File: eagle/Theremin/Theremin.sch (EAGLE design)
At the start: 15 parts, among them Q6 2N3904, Q7 2N3904, Q8 2N3904

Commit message: get everything committed to move to new machine
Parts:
- added C13: 22uF, SparkFun-Capacitors:CAP_POLPTH4
- added C14: 1800pF, SparkFun-Capacitors:CAPPTH3
- added C15: 6800pF, capacitor-wima:C5/3
- added D1, D3: 1N4004, diode:1N4004
- added L11: 47uH, marky-parts:SLOT-TEN-SIMPLE
- added L14: 22uH, marky-parts:DELEVAN-FIXED-INDUCTOR
- added U1: LM78L12, marky-parts:LM78L12
- added U2: LM79L12, marky-parts:LM79L12
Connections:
- new net N$10: C13.+, L11.IN$1, Q7.C
- new net N$11: L11.OUT$2, L14.P$1
- new net N$12: D3.A, U2.VIN
- new net N$13: D1.C, U1.VIN
- net GND: now also C13.-, C15.2, L11.P$1, L11.P$2, R17.1, U1.GND, U2.GND
- net N$4: now also C14.1, L14.P$2, Q6.C
- net N$8: now also R15.2
- net N$9: now also C14.2, C15.1
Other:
- moved on the sheet: C16, C17, C18, Q6, Q7, Q8, R15, R16, R17, R18, R19, R20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

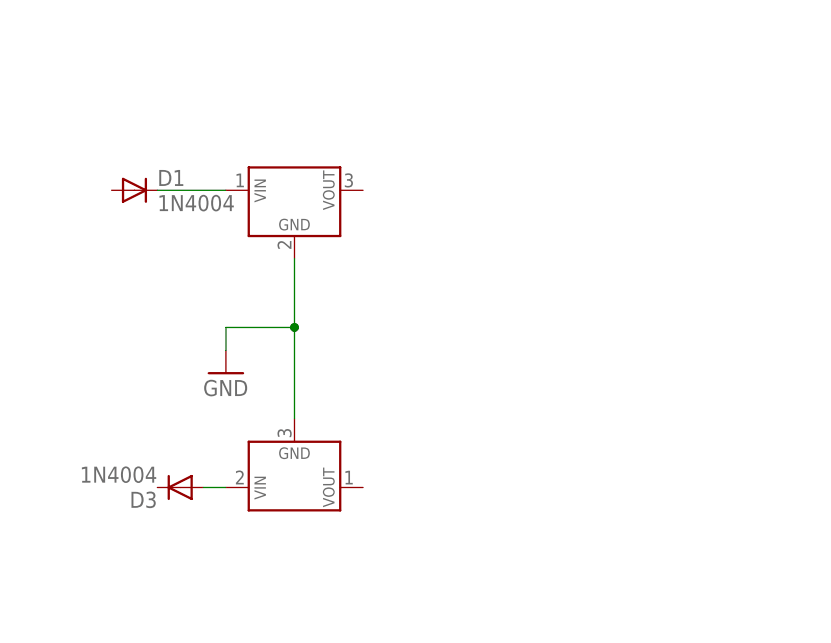
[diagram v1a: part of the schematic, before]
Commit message: Add big capacitors to theremin power supply
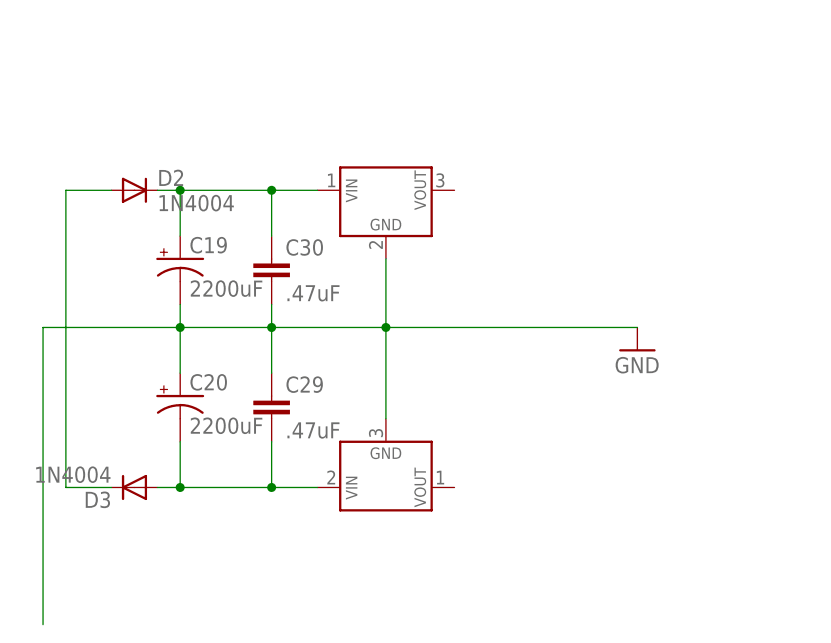
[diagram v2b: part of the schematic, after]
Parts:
- added C19, C20: 2200uF, marky-parts:1CM-RADIAL-CAP-POL
- added C29, C30: .47uF, SparkFun-Capacitors:CAP_
- renumbered D1 to D2
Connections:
- new net N$14: D2.A, D3.C
- net GND: now also C19.-, C20.+, C29.1, C30.2
- net N$12: now also C20.-, C29.2
- net N$13: now also C19.+, C30.1
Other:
- moved on the sheet: D3
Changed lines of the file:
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@@
 <setting verticaltext="up"/>
 </settings>
-<grid distance="0.1" unitdist="inch" unit="inch" style="lines" multiple="1" display="yes" altdistance="0.01" altunitdist="inch" altunit="inch"/>
+<grid distance="0.1" unitdist="inch" unit="inch" style="lines" multiple="1" display="no" altdistance="0.01" altunitdist="inch" altunit="inch"/>
 <layers>
 <layer number="1" name="Top" color="4" fill="1" visible="no" active="no"/>
@@
 <part name="U2" library="marky-parts" deviceset="LM79L12" device=""/>
 <part name="U1" library="marky-parts" deviceset="LM78L12" device=""/>
-<part name="D1" library="diode" deviceset="1N4004" device=""/>
+<part name="D2" library="diode" deviceset="1N4004" device=""/>
+<part name="C19" library="marky-parts" deviceset="1CM-RADIAL-CAP-POL" device="" value="2200uF"/>
+<part name="C20" library="marky-parts" deviceset="1CM-RADIAL-CAP-POL" device="" value="2200uF"/>
+<part name="C30" library="SparkFun-Capacitors" deviceset="CAP" device="_" value=".47uF"/>
+<part name="C29" library="SparkFun-Capacitors" deviceset="CAP" device="_" value=".47uF"/>
 </parts>
 <sheets>
@@
 <instance part="GND6" gate="1" x="157.48" y="120.65"/>
 <instance part="C14" gate="G$1" x="170.18" y="101.6"/>
-<instance part="D3" gate="1" x="17.78" y="43.18" rot="R180"/>
-<instance part="GND7" gate="1" x="22.86" y="55.88"/>
-<instance part="U2" gate="G$1" x="30.48" y="43.18"/>
-<instance part="U1" gate="G$1" x="30.48" y="76.2"/>
-<instance part="D1" gate="1" x="12.7" y="76.2"/>
+<instance part="D3" gate="1" x="12.7" y="43.18" rot="R180"/>
+<instance part="GND7" gate="1" x="68.58" y="58.42"/>
+<instance part="U2" gate="G$1" x="40.64" y="43.18"/>
+<instance part="U1" gate="G$1" x="40.64" y="76.2"/>
+<instance part="D2" gate="1" x="12.7" y="76.2"/>
+<instance part="C19" gate="G$1" x="17.78" y="68.58"/>
+<instance part="C20" gate="G$1" x="17.78" y="53.34"/>
+<instance part="C30" gate="G$1" x="27.94" y="66.04"/>
+<instance part="C29" gate="G$1" x="27.94" y="50.8"/>
 </instances>
 <busses>
@@
 <segment>
 <pinref part="U2" gate="G$1" pin="GND"/>
-<wire x1="30.48" y1="50.8" x2="30.48" y2="60.96" width="0.1524" layer="91"/>
-<wire x1="30.48" y1="60.96" x2="22.86" y2="60.96" width="0.1524" layer="91"/>
+<wire x1="40.64" y1="50.8" x2="40.64" y2="60.96" width="0.1524" layer="91"/>
 <pinref part="GND7" gate="1" pin="GND"/>
-<wire x1="22.86" y1="60.96" x2="22.86" y2="58.42" width="0.1524" layer="91"/>
+<wire x1="40.64" y1="60.96" x2="68.58" y2="60.96" width="0.1524" layer="91"/>
 <pinref part="U1" gate="G$1" pin="GND"/>
-<wire x1="30.48" y1="68.58" x2="30.48" y2="60.96" width="0.1524" layer="91"/>
-<junction x="30.48" y="60.96"/>
+<wire x1="40.64" y1="68.58" x2="40.64" y2="60.96" width="0.1524" layer="91"/>
+<junction x="40.64" y="60.96"/>
+<pinref part="C20" gate="G$1" pin="+"/>
+<pinref part="C19" gate="G$1" pin="-"/>
+<wire x1="17.78" y1="55.88" x2="17.78" y2="60.96" width="0.1524" layer="91"/>
+<wire x1="17.78" y1="60.96" x2="17.78" y2="63.5" width="0.1524" layer="91"/>
+<wire x1="40.64" y1="60.96" x2="27.94" y2="60.96" width="0.1524" layer="91"/>
+<wire x1="27.94" y1="60.96" x2="17.78" y2="60.96" width="0.1524" layer="91"/>
+<wire x1="17.78" y1="60.96" x2="2.54" y2="60.96" width="0.1524" layer="91"/>
+<wire x1="2.54" y1="60.96" x2="2.54" y2="27.94" width="0.1524" layer="91"/>
+<junction x="17.78" y="60.96"/>
+<pinref part="C29" gate="G$1" pin="1"/>
+<pinref part="C30" gate="G$1" pin="2"/>
+<wire x1="27.94" y1="55.88" x2="27.94" y2="60.96" width="0.1524" layer="91"/>
+<junction x="27.94" y="60.96"/>
+<wire x1="27.94" y1="60.96" x2="27.94" y2="63.5" width="0.1524" layer="91"/>
 </segment>
 </net>
@@
 <pinref part="U2" gate="G$1" pin="VIN"/>
 <pinref part="D3" gate="1" pin="A"/>
-<wire x1="22.86" y1="43.18" x2="20.32" y2="43.18" width="0.1524" layer="91"/>
+<wire x1="33.02" y1="43.18" x2="27.94" y2="43.18" width="0.1524" layer="91"/>
+<pinref part="C20" gate="G$1" pin="-"/>
+<wire x1="27.94" y1="43.18" x2="17.78" y2="43.18" width="0.1524" layer="91"/>
+<wire x1="17.78" y1="43.18" x2="15.24" y2="43.18" width="0.1524" layer="91"/>
+<wire x1="17.78" y1="48.26" x2="17.78" y2="43.18" width="0.1524" layer="91"/>
+<junction x="17.78" y="43.18"/>
+<pinref part="C29" gate="G$1" pin="2"/>
+<wire x1="27.94" y1="43.18" x2="27.94" y2="48.26" width="0.1524" layer="91"/>
+<junction x="27.94" y="43.18"/>
 </segment>
 </net>
 <net name="N$13" class="0">
 <segment>
-<pinref part="D1" gate="1" pin="C"/>
+<pinref part="D2" gate="1" pin="C"/>
 <pinref part="U1" gate="G$1" pin="VIN"/>
-<wire x1="15.24" y1="76.2" x2="22.86" y2="76.2" width="0.1524" layer="91"/>
-</segment>
-</net>
+<wire x1="15.24" y1="76.2" x2="17.78" y2="76.2" width="0.1524" layer="91"/>
+<pinref part="C19" gate="G$1" pin="+"/>
+<wire x1="17.78" y1="76.2" x2="27.94" y2="76.2" width="0.1524" layer="91"/>
+<wire x1="27.94" y1="76.2" x2="33.02" y2="76.2" width="0.1524" layer="91"/>
+<wire x1="17.78" y1="71.12" x2="17.78" y2="76.2" width="0.1524" layer="91"/>
+<junction x="17.78" y="76.2"/>
+<pinref part="C30" gate="G$1" pin="1"/>
+<wire x1="27.94" y1="71.12" x2="27.94" y2="76.2" width="0.1524" layer="91"/>
+<junction x="27.94" y="76.2"/>
+</segment>
+</net>
+<net name="N$14" class="0">
+<segment>
+<pinref part="D3" gate="1" pin="C"/>
+<wire x1="10.16" y1="43.18" x2="5.08" y2="43.18" width="0.1524" layer="91"/>
+<wire x1="5.08" y1="43.18" x2="5.08" y2="76.2" width="0.1524" layer="91"/>
+<pinref part="D2" gate="1" pin="A"/>
+<wire x1="5.08" y1="76.2" x2="10.16" y2="76.2" width="0.1524" layer="91"/>
+</segment>
+</net>

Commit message: Added Variable Pitch Oscillator cleaned up layout of schematic
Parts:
- added C1: 3300pF, marky-parts:CAP-9M-RADIAL
- added C2: 15pF, SparkFun-Capacitors:CAPPTH
- added C3: 0.01uF, marky-parts:CAP-5M-RADIAL
- added C4: 1uF, SparkFun-Passives:CAP_POLPTH2
- added L12: 47uH, marky-parts:DELEVAN-FIXED-INDUCTOR
- added L5: 47uH, marky-parts:SLOT-TEN-SIMPLE
- added Q1, Q2: 2N3904, transistor:2N3904
- added R1, R4: 1K, SparkFun-Resistors:RESISTORPTH-1/4W
- added R2: 2.2K, SparkFun-Resistors:RESISTORPTH-1/4W
- added R3: 47K, SparkFun-Resistors:RESISTORPTH-1/4W
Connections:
- new net 5V: C1.1, C13.+, C3.2, C4.+, L11.IN$1, L5.IN$1, Q2.C, Q7.C, R3.2
- new net N$16: Q1.B, R1.2
- new net N$17: C1.2, C2.1, C3.1, L12.P$2, Q1.C
- new net N$18: Q1.E, Q2.E, R2.2
- new net N$19: Q2.B, R3.1, R4.1
- new net N$20: C2.2
- net -12V: now also R2.1
- net GND: now also C4.-, L5.P$1, L5.P$2, R1.1, R4.2
- net N$10: now also L12.P$1, L5.OUT$2; no longer C13.+, L11.IN$1, Q7.C
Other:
- note added: "Power Supply"
- note added: "VARIABLE PITCH OSCILLATOR"
- note added: "Volume Antenna Circuit"
- note added: "to Pitch Antenna"

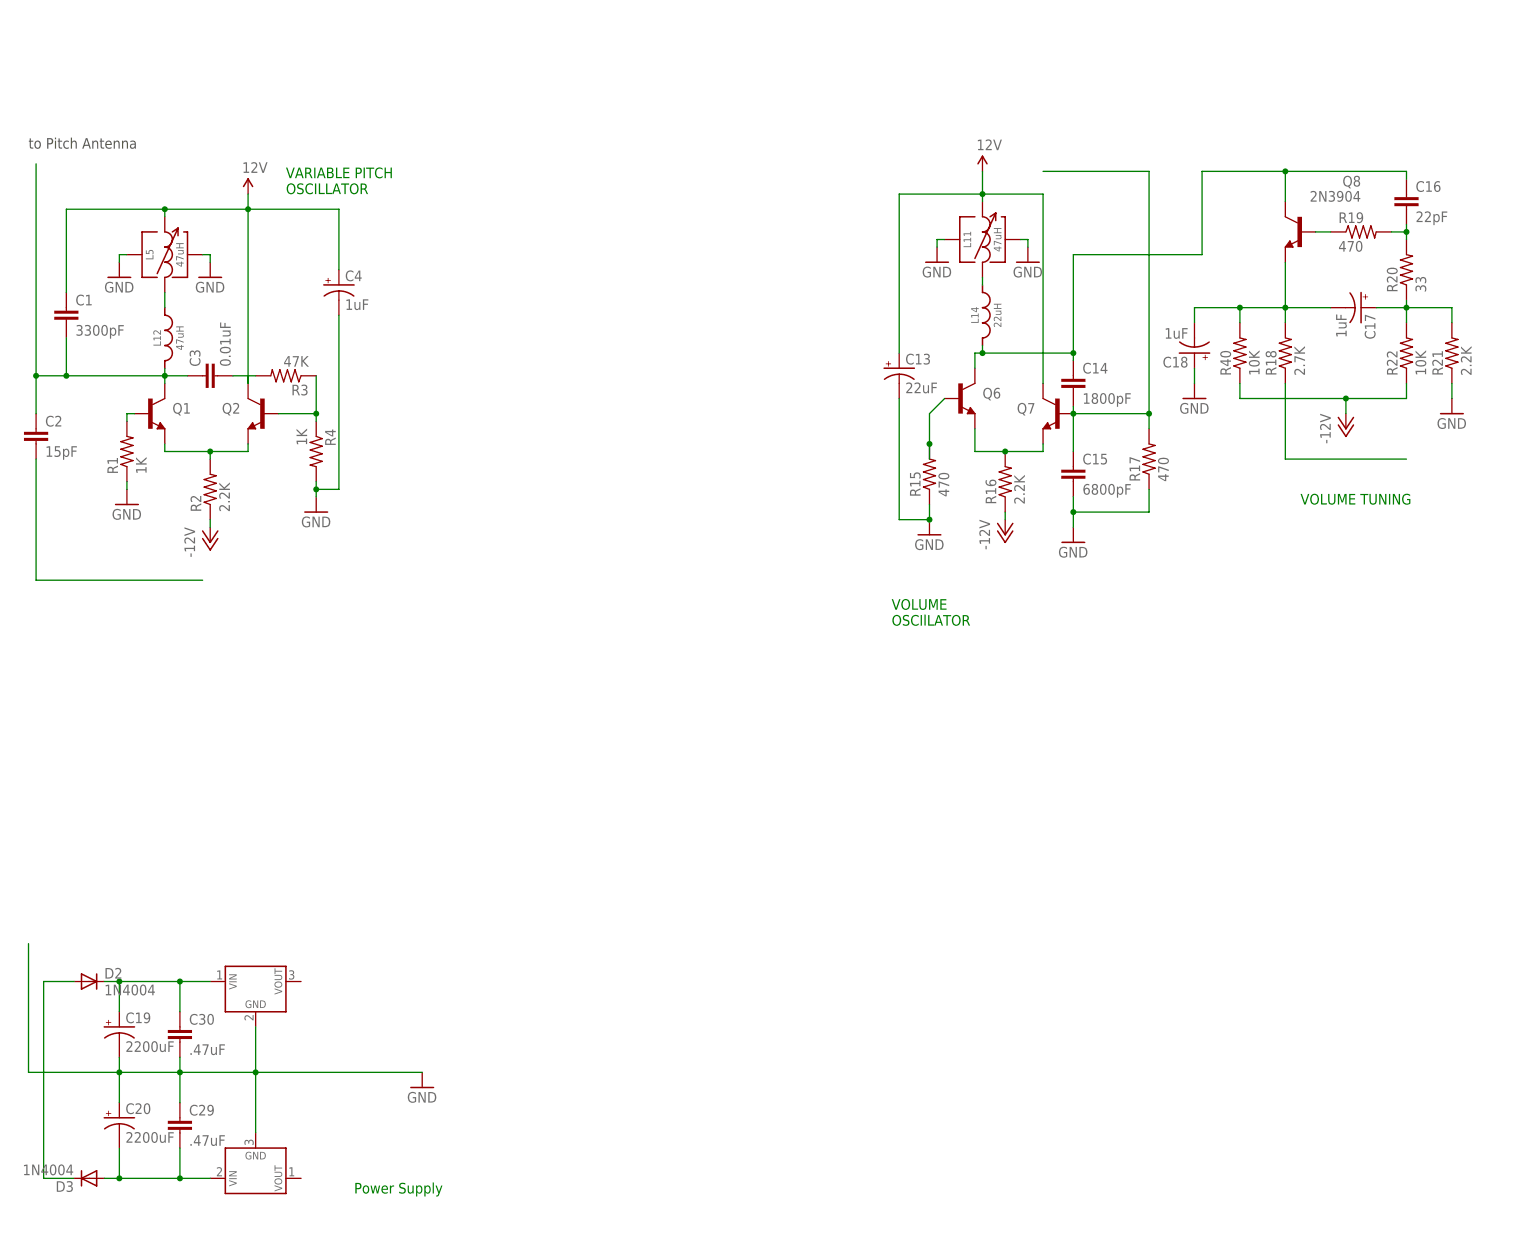
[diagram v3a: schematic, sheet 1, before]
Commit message: Added LM13600, VCA Processor, headers
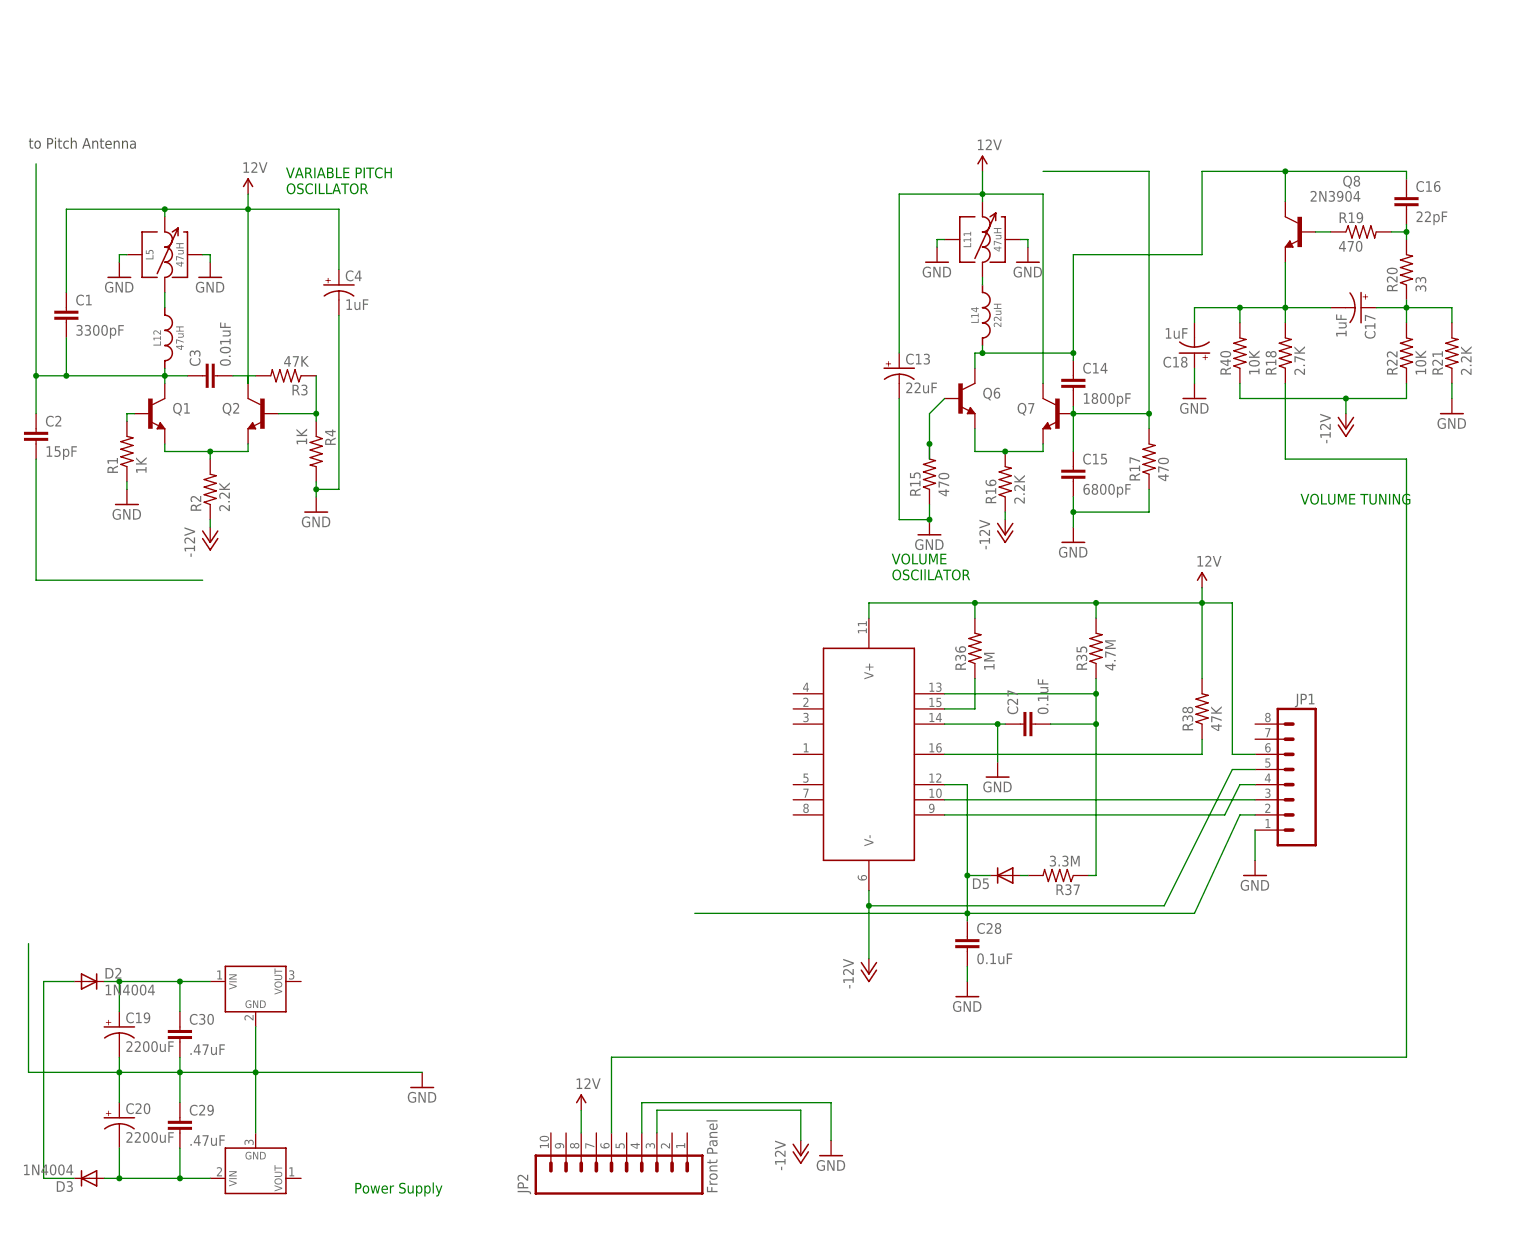
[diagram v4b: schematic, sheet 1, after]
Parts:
- added C27, C28: 0.1uF, SparkFun-Capacitors:CAPPTH
- added D5: (no value), SparkFun-DiscreteSemi:DIODE1N4148
- added JP1: (no value), SparkFun-Connectors:M081X08
- added JP2: Front Panel, SparkFun-Connectors:M10LOCK_LONGPADS
- added R35: 4.7M, SparkFun-Passives:RESISTOREZ
- added R36: 1M, SparkFun-Passives:RESISTOREZ
- added R37: 3.3M, SparkFun-Passives:RESISTOREZ
- added R38: 47K, SparkFun-Passives:RESISTOREZ
- added U3: (no value), marky-parts:LM13600
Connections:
- new net N$21: R38.1, U3.BIAS-IN-B
- new net N$22: JP1.3, U3.B-IN-B
- new net N$23: JP1.4, U3.B-OUT-B
- new net N$24: C28.1, D5.C, JP1.2, U3.OUT-B
- new net N$25: D5.A, R37.2
- new net N$26: C27.2, R35.1, R37.1, U3.IN-MINUS-B
- new net N$28: R36.1, U3.DIODE-BIAS-B
- net -12V: now also JP1.5, JP2.3, U3.V-
- net 5V: now also JP1.6, JP2.8, R35.2, R36.2, R38.2, U3.V+
- net GND: now also C27.1, C28.2, JP1.1, JP2.4, U3.IN-PLUS-B
- net N$7: now also JP2.6
